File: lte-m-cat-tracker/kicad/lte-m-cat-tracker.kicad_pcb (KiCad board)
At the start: 2 copper layers, 30 x 35 mm, 39 parts, among them J1 JST-GH-1.25mm-2P, J2 USB-C-16P, SW1 MSK12C02-HB, U1 SIM7080G-M, U2 ESP32-C3, U3 LIS2DW12TR, U4 TP4056, U5 XC6220B331MR-G, U6 TXB0104RGYR, Y1 7D040000M01 40MHz 12pF

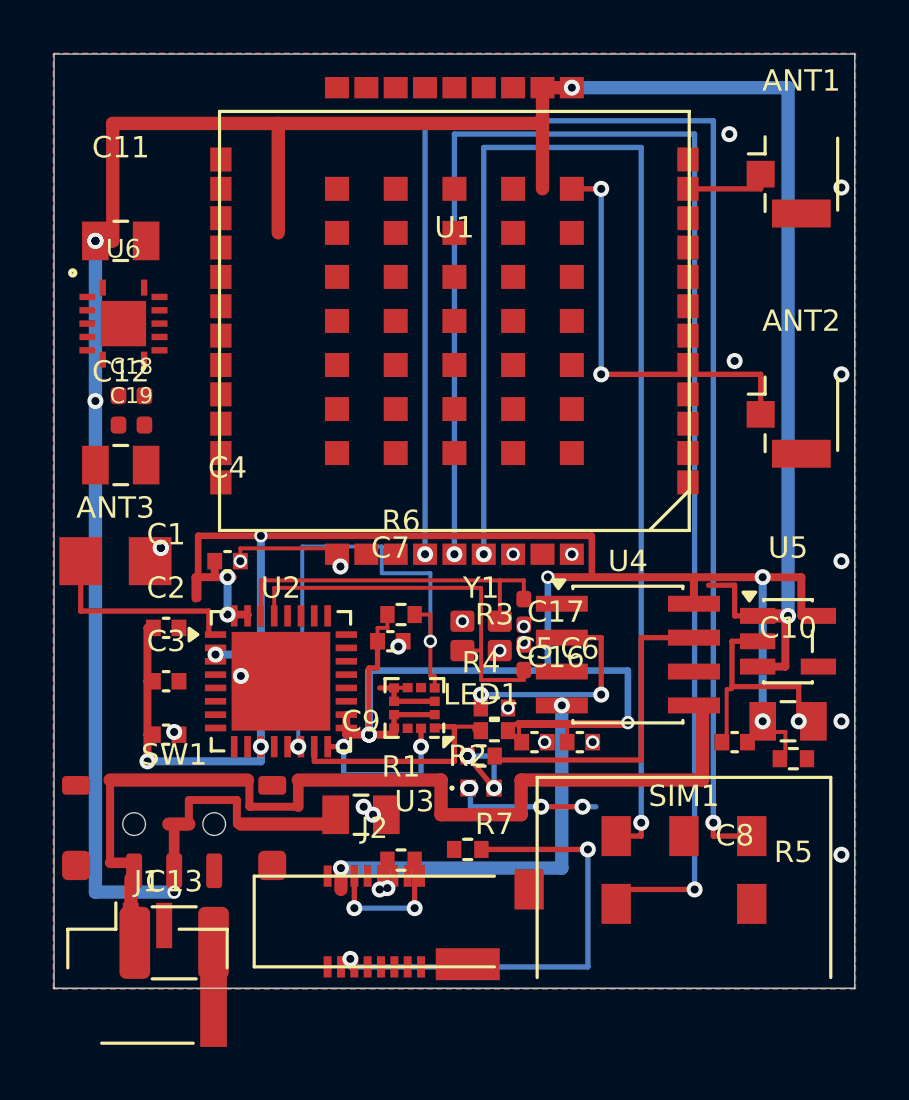
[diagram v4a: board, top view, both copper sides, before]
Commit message: Freeroutingで自動配線358セグメント取り込み・未配線86→4本・真の短絡0
- DSNエクスポート(pcbnew Python)→freerouting 2.1.0→SES自作パーサで注入
- ヘッドレスImportSpecctraSESが動かないため直接segment/via変換方式を確立
- 残4本(SIM_RXD/SIM_DATA/SIM_TXD_33/SIM_RXD_33)はU6周辺混雑部でGUI配線へ
- DRC: 違反241・shorting4件は全てネットvsNCパッド型(電気的無害)・dangling0

Co-Authored-By: Claude Fable 5 <noreply@anthropic.com>
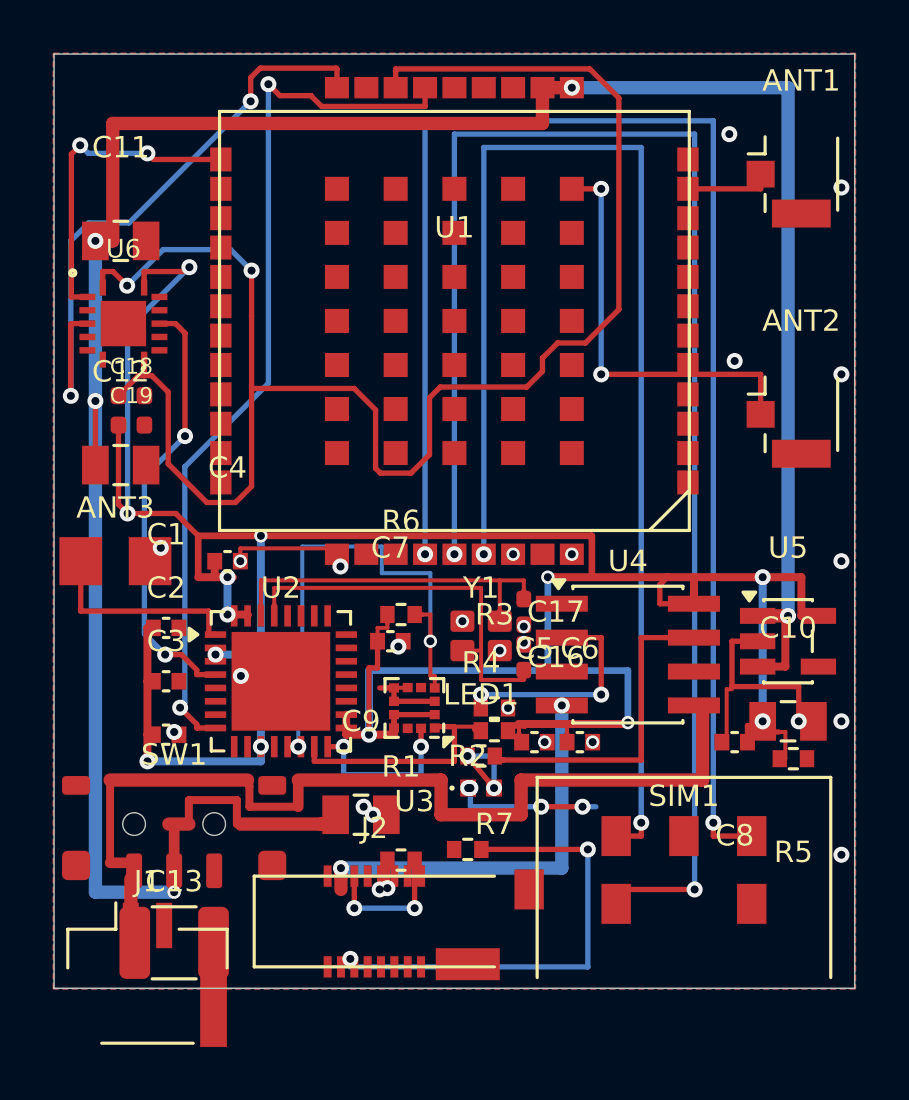
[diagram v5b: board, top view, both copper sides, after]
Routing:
- net VDD_EXT: track 0.00 -> 62.9 mm, vias 0 -> 2
- net SIM_PWRKEY: track 0.00 -> 33.4 mm, vias 0 -> 2
- net +3.3V: track 95.0 -> 120.9 mm, vias 12 -> 13
- net SIM_STATUS: track 0.00 -> 23.0 mm, vias 0 -> 2
- net SIM_STATUS_33: track 0.00 -> 16.4 mm, vias 0 -> 2
- net SIM_TXD: track 0.00 -> 11.9 mm, vias 0 -> 2
- net VBAT_SW: track 101.6 -> 96.6 mm, vias 6 -> 5
- net VBAT: track 35.8 -> 37.2 mm
- net XTAL_P: track 12.3 -> 13.4 mm
- net XTAL_N: track 14.0 -> 14.9 mm
- net LED_ANODE: vias 3 -> 2
- net GND: vias 32 -> 31

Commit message: BOM/CPL再生成・未実装だったC14/C15をPCBへ追加（BOM⇔CPL完全一致41部品）
- C14/C15(VBAT_SWパスコン)が回路図のみでPCB未実装と発見→(25.5,8.0)/(25.5,9.2)へ配置
- BOMにU6(C400708)とC14/C15/C18/C19追加・CPLはkicad-cli posから機械生成
- DRC: 違反240・真の短絡0

Co-Authored-By: Claude Fable 5 <noreply@anthropic.com>
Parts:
- added C14: 100nF, lte-m-custom:C_0402, F.Cu at (25.5, 8.00)
- added C15: 100nF, lte-m-custom:C_0402, F.Cu at (25.5, 9.20)
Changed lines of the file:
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@@
+		(embedded_fonts no)
+	)
+	(footprint "lte-m-custom:C_0402"
+		(layer "F.Cu")
+		(at 25.5 9.2)
+		(property "Reference" "C15"
+			(at 0 -1.1 0)
+			(layer "F.SilkS")
+			(effects
+				(font
+					(size 0.6 0.6)
+					(thickness 0.1)
+				)
+			)
+		)
+		(property "Value" "100nF"
+			(at 0 1.1 0)
+			(layer "F.Fab")
+			(effects
+				(font
+					(size 0.6 0.6)
+					(thickness 0.1)
+				)
+			)
+		)
+		(property "Datasheet" ""
+			(at 0 0 0)
+			(layer "F.Fab")
+			(hide yes)
+			(effects
+				(font
+					(size 1.27 1.27)
+				)
+			)
+		)
+		(property "Description" ""
+			(at 0 0 0)
+			(layer "F.Fab")
+			(hide yes)
+			(effects
+				(font
+					(size 1.27 1.27)
+				)
+			)
+		)
+		(attr smd)
+		(duplicate_pad_numbers_are_jumpers no)
+		(fp_rect
+			(start -0.93 -0.47)
+			(end 0.93 0.47)
+			(stroke
+				(width 0.05)
+				(type default)
+			)
+			(fill no)
+			(layer "F.CrtYd")
+		)
+		(pad "1" smd roundrect
+			(at -0.485 0)
+			(size 0.59 0.64)
+			(layers "F.Cu" "F.Mask" "F.Paste")
+			(roundrect_rratio 0.25)
+			(net "VBAT_SW")
+		)
+		(pad "2" smd roundrect
+			(at 0.485 0)
+			(size 0.59 0.64)
+			(layers "F.Cu" "F.Mask" "F.Paste")
+			(roundrect_rratio 0.25)
+			(net "GND")
+		)
 		(embedded_fonts no)
 	)
@@
 		)
 		(embedded_fonts no)
+	)
+	(footprint "lte-m-custom:C_0402"
+		(layer "F.Cu")
+		(at 25.5 8)
+		(property "Reference" "C14"
+			(at 0 -1.1 0)
+			(layer "F.SilkS")
+			(effects
+				(font
+					(size 0.6 0.6)
+					(thickness 0.1)
+				)
+			)
+		)
+		(property "Value" "100nF"
+			(at 0 1.1 0)
+			(layer "F.Fab")
+			(effects
+				(font
+					(size 0.6 0.6)
+					(thickness 0.1)
+				)
+			)
+		)
+		(property "Datasheet" ""
+			(at 0 0 0)
+			(layer "F.Fab")
+			(hide yes)
+			(effects
+				(font
+					(size 1.27 1.27)
+				)
+			)
+		)
+		(property "Description" ""
+			(at 0 0 0)
+			(layer "F.Fab")
+			(hide yes)
+			(effects
+				(font
+					(size 1.27 1.27)
+				)
+			)
+		)
+		(attr smd)
+		(duplicate_pad_numbers_are_jumpers no)
+		(fp_rect
+			(start -0.93 -0.47)
+			(end 0.93 0.47)
+			(stroke
+				(width 0.05)
+				(type default)
+			)
+			(fill no)
+			(layer "F.CrtYd")
+		)
+		(pad "1" smd roundrect
+			(at -0.485 0)
+			(size 0.59 0.64)
+			(layers "F.Cu" "F.Mask" "F.Paste")
+			(roundrect_rratio 0.25)
+			(net "VBAT_SW")
+		)
+		(pad "2" smd roundrect
+			(at 0.485 0)
+			(size 0.59 0.64)
+			(layers "F.Cu" "F.Mask" "F.Paste")
+			(roundrect_rratio 0.25)
+			(net "GND")
+		)
+		(embedded_fonts no)

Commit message: C14/C15のVBAT_SWタップ接続・GND孤島の大半解消（違反237・真の短絡0）
- C14/C15→B.Cu幹線タップ(SIM_CLK衝突を修正済み)・C18/C19 GND接続+ビア
- U1 pad37/67インパッドビア。pad70はSIM_RST衝突のためGUI送り
- 残: 信号4本+GND孤島6件+NCパッド整形=全てGUI作業として明細化

Co-Authored-By: Claude Fable 5 <noreply@anthropic.com>
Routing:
- net VBAT_SW: track 96.6 -> 101.1 mm, vias 5 -> 6
- net GND: track 22.8 -> 23.9 mm, vias 31 -> 35
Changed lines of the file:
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@@
+	)
+	(segment
+		(start 3.385 12.8)
+		(end 3.385 13.9)
+		(width 0.3)
+		(layer "F.Cu")
+		(net "GND")
 	)
 	(segment
@@
 	)
 	(via
+		(at 16.1 1.26)
+		(size 0.6)
+		(drill 0.3)
+		(layers "F.Cu" "B.Cu")
+		(net "GND")
+	)
+	(via
 		(at 25.3 3)
 		(size 0.6)
@@
 	(via
 		(at 27.9 25)
+		(size 0.6)
+		(drill 0.3)
+		(layers "F.Cu" "B.Cu")
+		(net "GND")
+	)
+	(via
+		(at 15 13.3)
 		(size 0.6)
 		(drill 0.3)
@@
 	)
 	(via
+		(at 10.6 13.3)
+		(size 0.6)
+		(drill 0.3)
+		(layers "F.Cu" "B.Cu")
+		(net "GND")
+	)
+	(via
 		(at 17.6 22.05)
 		(size 0.5)
@@
 	(via
 		(at 29.5 12)
+		(size 0.6)
+		(drill 0.3)
+		(layers "F.Cu" "B.Cu")
+		(net "GND")
+	)
+	(via
+		(at 3.385 13.35)
 		(size 0.6)
 		(drill 0.3)
@@
 	)
 	(segment
+		(start 25.015 8)
+		(end 25.015 7.15)
+		(width 0.3)
+		(layer "F.Cu")
+		(net "VBAT_SW")
+	)
+	(segment
 		(start 2.2 7)
 		(end 1.55 7)
@@
 	)
 	(segment
+		(start 25.015 9.2)
+		(end 25.015 8)
+		(width 0.3)
+		(layer "F.Cu")
+		(net "VBAT_SW")
+	)
+	(segment
 		(start 10 28.85)
 		(end 10.55 28.85)
@@
 	)
 	(segment
+		(start 25.015 7.15)
+		(end 25.45 7.15)
+		(width 0.3)
+		(layer "F.Cu")
+		(net "VBAT_SW")
+	)
+	(segment
 		(start 27.4 21.05)
 		(end 26.363 21.05)
@@
 	)
 	(via
+		(at 25.45 7.15)
+		(size 0.6)
+		(drill 0.3)
+		(layers "F.Cu" "B.Cu")
+		(net "VBAT_SW")
+	)
+	(via
 		(at 19.4 1.26)
 		(size 0.6)
@@
 		(width 0.5)
 		(layer "B.Cu")
+		(net "VBAT_SW")
+	)
+	(segment
+		(start 25.45 7.15)
+		(end 27.5 7.15)
+		(width 0.5)
+		(layer "B.Cu")

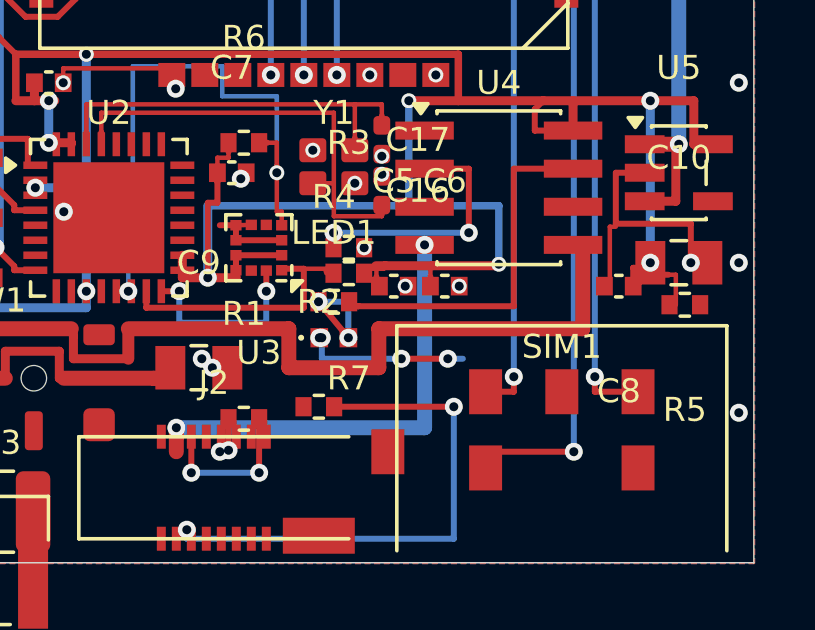
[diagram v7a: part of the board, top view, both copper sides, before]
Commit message: 致命2-4のネット定義実装: CHIP_EN(R5+C20)・GPIO2プルアップ(R8)・USB書込経路(J2 D±↔GPIO18/19)
- 部品2点追加(C20/R8)・配置DRCクリア・BOM/CPL再生成43部品一致
- 配線と回路図反映は次回（ratlines 19本にfreerouting再実行で対応予定）

Co-Authored-By: Claude Fable 5 <noreply@anthropic.com>
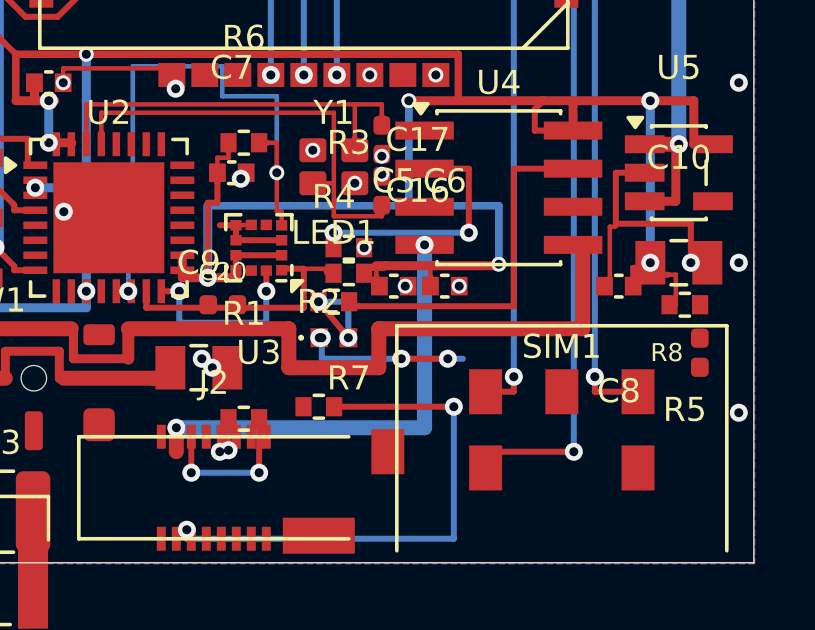
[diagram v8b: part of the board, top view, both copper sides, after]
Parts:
- added C20: 100nF, lte-m-custom:C_0402, F.Cu at (12.3, 26.4)
- added R8: 10k, lte-m-custom:C_0402, F.Cu at (28.2, 28.0)
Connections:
- J2 pad A6: (no net) -> USB_DP
- J2 pad A7: (no net) -> USB_DN
- J2 pad B6: (no net) -> USB_DP
- J2 pad B7: (no net) -> USB_DN
- R5 pad 1: (no net) -> CHIP_EN
- U2 pad 25: (no net) -> USB_DN
- U2 pad 26: (no net) -> USB_DP
- U2 pad 6: (no net) -> ESP_GPIO2
- U2 pad 7: (no net) -> CHIP_EN
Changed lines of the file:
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@@
 			(size 0.3 0.8)
 			(layers "F.Cu" "F.Mask" "F.Paste")
+			(net "USB_DP")
 			(thermal_bridge_angle 45)
 		)
@@
 			(size 0.3 0.8)
 			(layers "F.Cu" "F.Mask" "F.Paste")
+			(net "USB_DN")
 			(thermal_bridge_angle 45)
 		)
@@
 			(size 0.3 0.8)
 			(layers "F.Cu" "F.Mask" "F.Paste")
+			(net "USB_DP")
 			(thermal_bridge_angle 45)
 		)
@@
 			(size 0.3 0.8)
 			(layers "F.Cu" "F.Mask" "F.Paste")
+			(net "USB_DN")
 			(thermal_bridge_angle 45)
 		)
@@
 		(embedded_fonts no)
 	)
+	(footprint "lte-m-custom:C_0402"
+		(layer "F.Cu")
+		(at 12.3 26.4)
+		(property "Reference" "C20"
+			(at 0 -1.1 0)
+			(layer "F.SilkS")
+			(effects
+				(font
+					(size 0.6 0.6)
+					(thickness 0.1)
+				)
+			)
+		)
+		(property "Value" "100nF"
+			(at 0 1.1 0)
+			(layer "F.Fab")
+			(effects
+				(font
+					(size 0.6 0.6)
+					(thickness 0.1)
+				)
+			)
+		)
+		(property "Datasheet" ""
+			(at 0 0 0)
+			(layer "F.Fab")
+			(hide yes)
+			(effects
+				(font
+					(size 1.27 1.27)
+				)
+			)
+		)
+		(property "Description" ""
+			(at 0 0 0)
+			(layer "F.Fab")
+			(hide yes)
+			(effects
+				(font
+					(size 1.27 1.27)
+				)
+			)
+		)
+		(attr smd)
+		(duplicate_pad_numbers_are_jumpers no)
+		(fp_rect
+			(start -0.93 -0.47)
+			(end 0.93 0.47)
+			(stroke
+				(width 0.05)
+				(type default)
+			)
+			(fill no)
+			(layer "F.CrtYd")
+		)
+		(pad "1" smd roundrect
+			(at -0.485 0)
+			(size 0.59 0.64)
+			(layers "F.Cu" "F.Mask" "F.Paste")
+			(roundrect_rratio 0.25)
+			(net "CHIP_EN")
+		)
+		(pad "2" smd roundrect
+			(at 0.485 0)
+			(size 0.59 0.64)
+			(layers "F.Cu" "F.Mask" "F.Paste")
+			(roundrect_rratio 0.25)
+			(net "GND")
+		)
+		(embedded_fonts no)
+	)
 	(footprint ""
 		(layer "F.Cu")
@@
 			(size 0.8 0.25)
 			(layers "F.Cu" "F.Mask" "F.Paste")
+			(net "ESP_GPIO2")
 			(thermal_bridge_angle 45)
 		)
@@
 			(size 0.8 0.25)
 			(layers "F.Cu" "F.Mask" "F.Paste")
+			(net "CHIP_EN")
 			(thermal_bridge_angle 45)
 		)
@@
 			(size 0.25 0.8)
 			(layers "F.Cu" "F.Mask" "F.Paste")
+			(net "USB_DN")
 			(thermal_bridge_angle 45)
 		)
@@
 			(size 0.25 0.8)
 			(layers "F.Cu" "F.Mask" "F.Paste")
+			(net "USB_DP")
 			(thermal_bridge_angle 45)
 		)
@@
 			(size 0.54 0.64)
 			(layers "F.Cu" "F.Mask" "F.Paste")
+			(net "CHIP_EN")
 			(thermal_bridge_angle 45)
 		)
@@
 		)
 		(embedded_fonts no)
+	)
+	(footprint "lte-m-custom:C_0402"
+		(layer "F.Cu")
+		(at 28.2 28 90)
+		(property "Reference" "R8"
+			(at 0 -1.1 0)
+			(layer "F.SilkS")
+			(effects
+				(font
+					(size 0.6 0.6)
+					(thickness 0.1)
+				)
+			)
+		)
+		(property "Value" "10k"
+			(at 0 1.1 0)
+			(layer "F.Fab")
+			(effects
+				(font
+					(size 0.6 0.6)
+					(thickness 0.1)
+				)
+			)
+		)
+		(property "Datasheet" ""
+			(at 0 0 0)
+			(layer "F.Fab")
+			(hide yes)
+			(effects
+				(font
+					(size 1.27 1.27)
+				)
+			)
+		)
+		(property "Description" ""
+			(at 0 0 0)
+			(layer "F.Fab")
+			(hide yes)
+			(effects
+				(font
+					(size 1.27 1.27)
+				)
+			)
+		)
+		(attr smd)
+		(duplicate_pad_numbers_are_jumpers no)
+		(fp_rect
+			(start -0.93 -0.47)
+			(end 0.93 0.47)
+			(stroke
+				(width 0.05)
+				(type default)
+			)
+			(fill no)
+			(layer "F.CrtYd")
+		)
+		(pad "1" smd roundrect
+			(at -0.485 0)
+			(size 0.59 0.64)
+			(layers "F.Cu" "F.Mask" "F.Paste")
+			(roundrect_rratio 0.25)
+			(net "ESP_GPIO2")
+		)
+		(pad "2" smd roundrect
+			(at 0.485 0)
+			(size 0.59 0.64)
+			(layers "F.Cu" "F.Mask" "F.Paste")
+			(roundrect_rratio 0.25)
+			(net "+3.3V")
+		)
+		(embedded_fonts no)
